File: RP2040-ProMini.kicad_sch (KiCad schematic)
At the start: 6 parts, among them J1 CONN_L, J2 CONN_R, J3 CONN_R2, J4 CONN_R3, J5 CONN_U, U1 RP2040

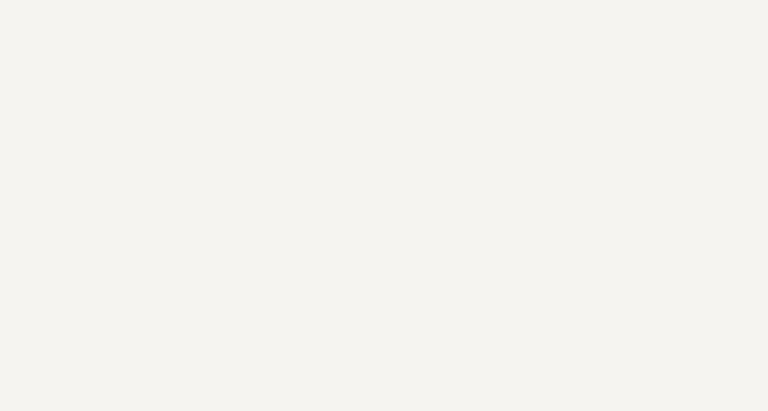
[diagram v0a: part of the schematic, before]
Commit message: Added basic power input
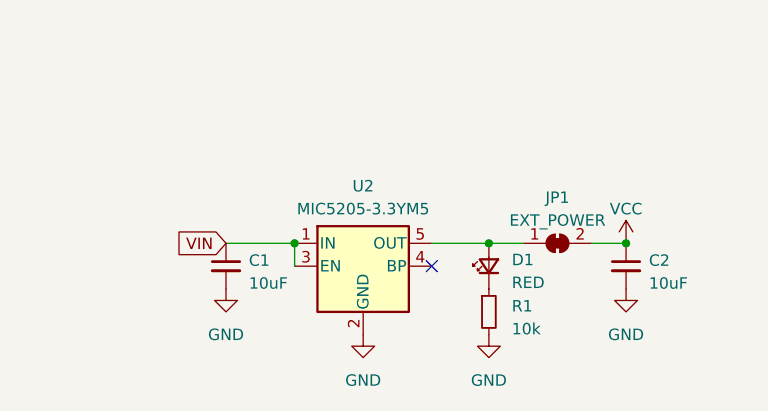
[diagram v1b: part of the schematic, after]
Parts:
- added C1, C2: 10uF, Capacitor_SMD:C_0805_2012Metric, symbol Device:C_Small
- added D1: RED, LED_SMD:LED_0603_1608Metric, symbol Device:LED_Small
- added JP1: EXT_POWER, Jumper:SolderJumper-2_P1.3mm_Bridged_RoundedPad1.0x1.5mm, symbol Jumper:SolderJumper_2_Bridged
- added R1: 10k, Resistor_SMD:R_0603_1608Metric, symbol Device:R_Small
- added U2: MIC5205-3.3YM5, Package_TO_SOT_SMD:SOT-23-5, symbol Regulator_Linear:MIC5205-3.3YM5
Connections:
- net GND: now also C1.2, C2.2, R1.2, U2.2 (GND)
- net VCC: now also C2.1, JP1.2 (B)
- net VIN: now also C1.1, U2.1 (IN), U2.3 (EN)
- new net: D1.2 (A), JP1.1 (A), U2.5 (OUT)
- new net: D1.1 (K), R1.1
- no-connect marks 0 -> 1

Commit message: Added whole bunch of things
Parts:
- added C10, C3, C4, C5, C6, C7, C8, C9: 100nF, Capacitor_SMD:C_0402_1005Metric, symbol Device:C_Small
- added C11, C12: 2.2uF, Capacitor_SMD:C_0603_1608Metric, symbol Device:C_Small
- added D2: RED, LED_SMD:LED_0603_1608Metric, symbol Device:LED_Small
- added Q1: AO3400A, Package_TO_SOT_SMD:SOT-23, symbol Transistor_FET:AO3400A
- added R2, R3, R4, R5, R6: 10k, Resistor_SMD:R_0402_1005Metric, symbol Device:R_Small
- added U3: W25Q128JVS, Package_SO:SOIC-8_5.23x5.23mm_P1.27mm, symbol Memory_Flash:W25Q128JVS
- added Y1: 12MHz, Crystal:Crystal_SMD_3225-4Pin_3.2x2.5mm, symbol Device:Crystal_GND24_Small
- R1: footprint Resistor_SMD:R_0603_1608Metric -> Resistor_SMD:R_0402_1005Metric
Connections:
- net VCC is gone; now on net +3.3V: C2.1, J2.4 (Pin_4), JP1.2 (B)
- net D13_SCK: now also Q1.1 (G)
- net D18_A4_SDA: now also R3.2
- net D19_A5_SCL: now also R2.2
- net GND: now also U1.19 (TESTEN), C10.2, C11.2, C12.2, C3.2, C4.2, C5.2, C6.2, C7.2, C8.2, C9.2, Q1.2 (S), U3.4 (GND), Y1.2, Y1.4
- net RESET: now also U1.26 (RUN), R5.2
- net USB_DP: now reaches J5.2 (Pin_2)
- net USB_DP: now also U1.47 (USB_DP)
- net USB_DM: now reaches J5.4 (Pin_4)
- net USB_DM: now also U1.46 (USB_DM)
- net SWCLK: now reaches J5.5 (Pin_5)
- net SWCLK: now also U1.24 (SWCLK), R4.2
- net SWD: now reaches J5.6 (Pin_6)
- net SWD: now also U1.25 (SWD)
- net +3.3V: now reaches U1.1 (IOVDD), U1.10 (IOVDD), U1.22 (IOVDD), U1.33 (IOVDD), U1.42 (IOVDD), U1.49 (IOVDD)
- net +3.3V: now also U1.43 (ADC_AVDD), U1.44 (VREG_IN), U1.48 (USB_VDD), C12.1, C3.1, C4.1, C5.1, C6.1, C7.1, C8.1, C9.1, D2.2 (A), R2.1, R3.1, R4.1, R5.1, U3.8 (VCC)
- net XIN: now reaches U1.20 (XIN)
- net XIN: now also Y1.1
- net XOUT: now reaches U1.21 (XOUT)
- net XOUT: now also Y1.3
- net +1V1: now reaches U1.23 (DVDD), U1.50 (DVDD)
- net +1V1: now also U1.45 (VREG_VOUT), C10.1, C11.1
- net QSPI_SD3: now reaches U1.51 (QSPI_SD3)
- net QSPI_SD3: now also U3.7 (IO3)
- net QSPI_SCLK: now reaches U1.52 (QSPI_SCLK)
- net QSPI_SCLK: now also U3.6 (CLK)
- net QSPI_SD0: now reaches U1.53 (QSPI_SD0)
- net QSPI_SD0: now also U3.5 (DI(IO0))
- net QSPI_SD2: now reaches U1.54 (QSPI_SD2)
- net QSPI_SD2: now also U3.3 (IO2)
- net QSPI_SD1: now reaches U1.55 (QSPI_SD1)
- net QSPI_SD1: now also U3.2 (DO(IO1))
- net QSPI_SS: now reaches U1.56 (QSPI_SS)
- net QSPI_SS: now also U3.1 (~{CS})
- new net: D2.1 (K), R6.1
- new net: Q1.3 (D), R6.2
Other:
- moved on the sheet: C1, C2, D1, J1, J2, J3, J4, J5, JP1, R1, U1, U2

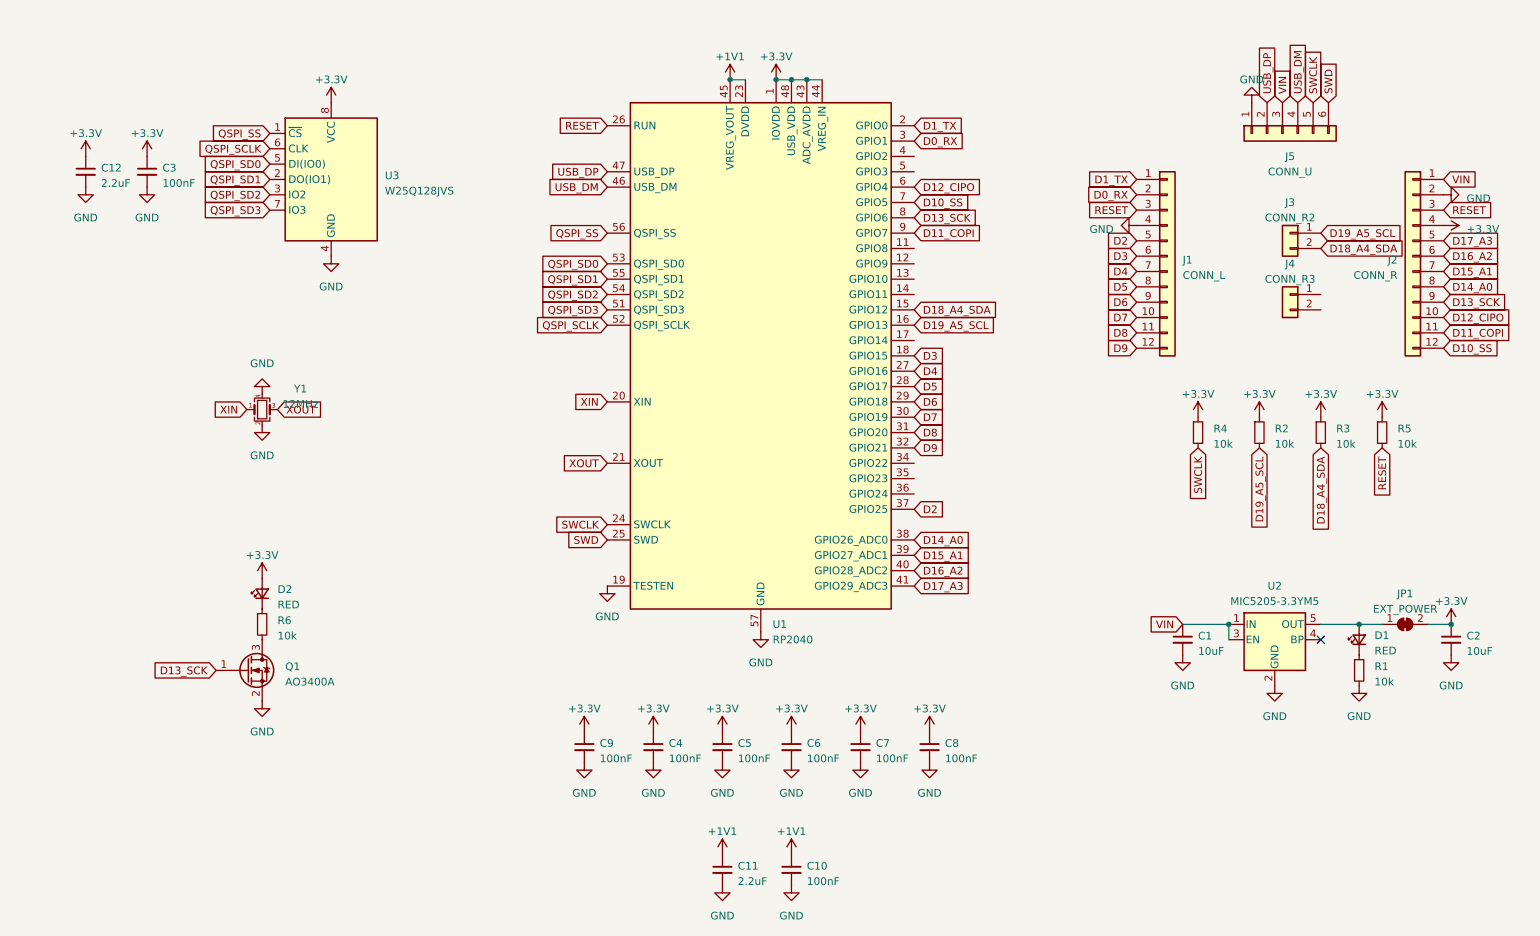
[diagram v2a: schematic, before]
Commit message: Removed 2-pin connector. Routed power traces and fills. Started to route traces.
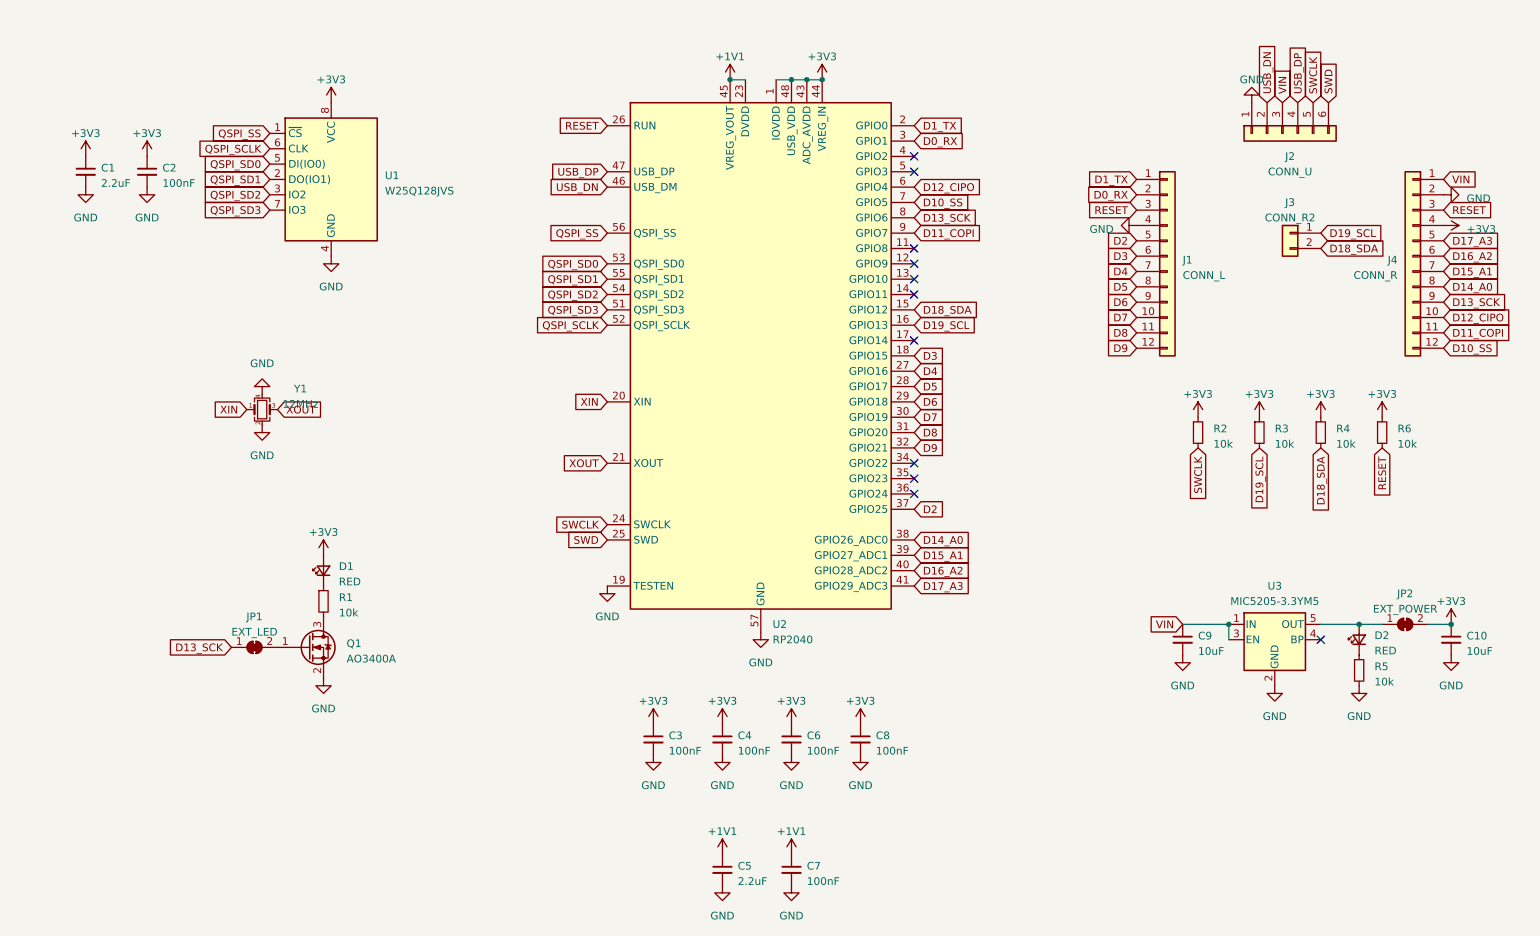
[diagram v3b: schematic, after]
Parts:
- removed C7, C9: 100nF, Capacitor_SMD:C_0402_1005Metric, symbol Device:C_Small
- removed J4: CONN_R3, Connector_PinHeader_2.54mm:PinHeader_1x02_P2.54mm_Vertical, symbol Connector_Generic:Conn_01x02
- added JP1: EXT_LED, Jumper:SolderJumper-2_P1.3mm_Bridged_RoundedPad1.0x1.5mm, symbol Jumper:SolderJumper_2_Bridged
- renumbered C12 to C1, C2 to C10, C3 to C2, C4 to C3, C5 to C4, C11 to C5, C10 to C7, C1 to C9, D2 to D1, D1 to D2, J5 to J2, J2 to J4, JP1 to JP2, R6 to R1, R4 to R2, R2 to R3, R3 to R4, R1 to R5, R5 to R6, U3 to U1, U1 to U2, U2 to U3
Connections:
- net D13_SCK: now also JP1.1 (A); no longer Q1.1 (G)
- net USB_DP: now also J2.4 (Pin_4); no longer J2.2 (Pin_2)
- net +3.3V renamed +3V3
- net D18_A4_SDA renamed D18_SDA
- net D19_A5_SCL renamed D19_SCL
- net USB_DM renamed USB_DN
- net USB_DN: now also J2.2 (Pin_2); no longer J2.4 (Pin_4)
- new net: JP1.2 (B), Q1.1 (G)
- no-connect marks 1 -> 11
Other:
- moved on the sheet: C3, C4, C6, C8, D1, Q1, R1

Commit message: Finished routing of the board.
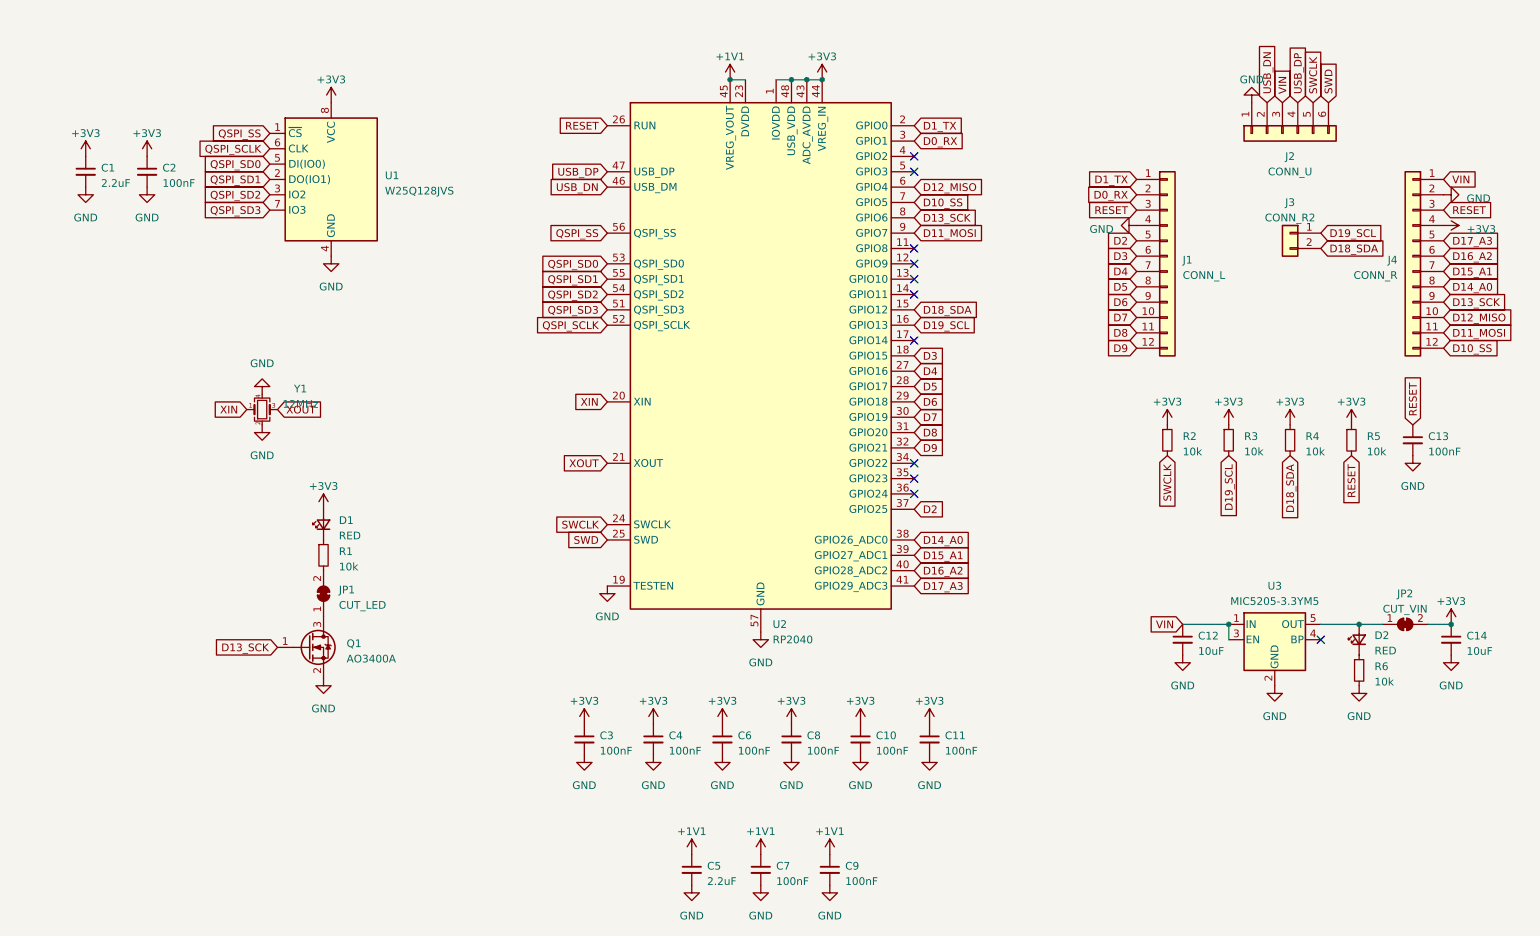
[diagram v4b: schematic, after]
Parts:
- added C11, C13, C3, C9: 100nF, Capacitor_SMD:C_0402_1005Metric, symbol Device:C_Small
- JP1: value EXT_LED -> CUT_LED
- JP2: value EXT_POWER -> CUT_VIN
- renumbered C8 to C10, C9 to C12, C10 to C14, C3 to C4, C4 to C6, C6 to C8, R6 to R5, R5 to R6
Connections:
- net +1V1: now also C9.1
- net +3V3: now also C11.1, C3.1
- net D13_SCK: now also Q1.1 (G); no longer JP1.1 (A)
- net GND: now also C11.2, C13.2, C3.2, C9.2
- net RESET: now also C13.1
- net at R1.2: now also JP1.2 (B); no longer Q1.3 (D)
- net D11_COPI renamed D11_MOSI
- net D12_CIPO renamed D12_MISO
- new net: JP1.1 (A), Q1.3 (D)
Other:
- moved on the sheet: C5, C7, D1, JP1, R1, R2, R3, R4, R5
